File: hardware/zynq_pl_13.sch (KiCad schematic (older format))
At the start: 1 part

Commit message: Added a few Todos.
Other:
- note added: "TODO: VCCO(2,5 V AFAIK)"
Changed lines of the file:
@@
 Text Label 7100 6100 2    60   ~ 0
 CAM_CTRL_1_P
+Text Notes 1050 1200 0    60   ~ 0
+TODO: VCCO(2,5 V AFAIK)
 $EndSCHEMATC

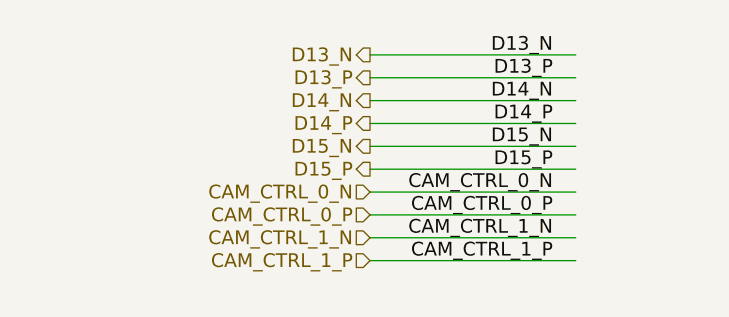
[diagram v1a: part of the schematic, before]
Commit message: Added decoupling Capacitors for the Zynq. Also added the 2,5 V Power supply.
The 2,5 V supply was implemented as LDO and is sourced by the 3,3 V Line.
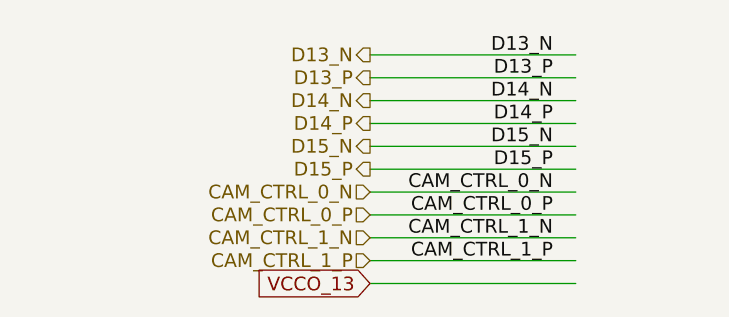
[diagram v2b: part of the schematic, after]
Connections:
- net labels added: VCCO_13
- wire segments 44 -> 45
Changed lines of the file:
@@
 Text Notes 1050 1200 0    60   ~ 0
 TODO: VCCO(2,5 V AFAIK)
+Text GLabel 6300 6200 0    60   Input ~ 0
+VCCO_13
+Wire Wire Line
+	6300 6200 7200 6200
 $EndSCHEMATC

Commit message: Started to route DDR3 Memory.
At first added missing Footprint for Reference- and Terminationvoltage Regulator. Added Powerplanes for GND and VCCO. Added decoupling Network to both DDR3 Memory Chips. There are more small caps, to support Memory from other Manufactors.
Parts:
- gave numbers to parts that had none: 1
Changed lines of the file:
@@
 $EndDescr
 $Comp
-L xc7z030sbg485 U?
+L xc7z030sbg485 U1
 U 2 1 596E7737
 P 7200 1200
-F 0 "U?" H 7400 1450 60  0000 L CNN
+F 0 "U1" H 7400 1450 60  0000 L CNN
 F 1 "xc7z030sbg485" H 7400 1350 60  0000 L CNN
 F 2 "footprints:SBG485_22x22_19.0x19.0mm_Pitch0.8mm" H 7200 1200 60  0001 C CNN

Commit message: Corrected two mistakes in the DDR Sheet. Changed bit sequence a bit to ease routing. Added more decoupling Caps Termination Voltage.
Mistakes: the Bank Address was not terminated. The Reset Line was connected like it's an terminated Signal. Reset should be connected through an PD Resistor to GND.
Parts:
- U1: Populate for CLG484(Z-7012s/Z-7015) (none) -> 1; Populate for SBGA485(Z-7030) (none) -> 1; Populated (none) -> 1; Source (none) -> SPEC
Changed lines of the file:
@@
 F 2 "footprints:SBG485_22x22_19.0x19.0mm_Pitch0.8mm" H 7200 1200 60  0001 C CNN
 F 3 "" H 7200 1200 60  0001 C CNN
+F 4 "1" H 7200 1200 60  0001 C CNN "Populated"
+F 5 "SPEC" H 7200 1200 60  0001 C CNN "Source"
+F 6 "1" H 7200 1200 60  0001 C CNN "Populate for SBGA485(Z-7030)"
+F 7 "1" H 7200 1200 60  0001 C CNN "Populate for CLG484(Z-7012s/Z-7015)"
 	2    7200 1200
 	1    0    0    -1
